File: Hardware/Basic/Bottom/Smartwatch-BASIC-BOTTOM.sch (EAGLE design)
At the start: 37 parts, among them U1 AD5242-SO16, U3 PCF8523

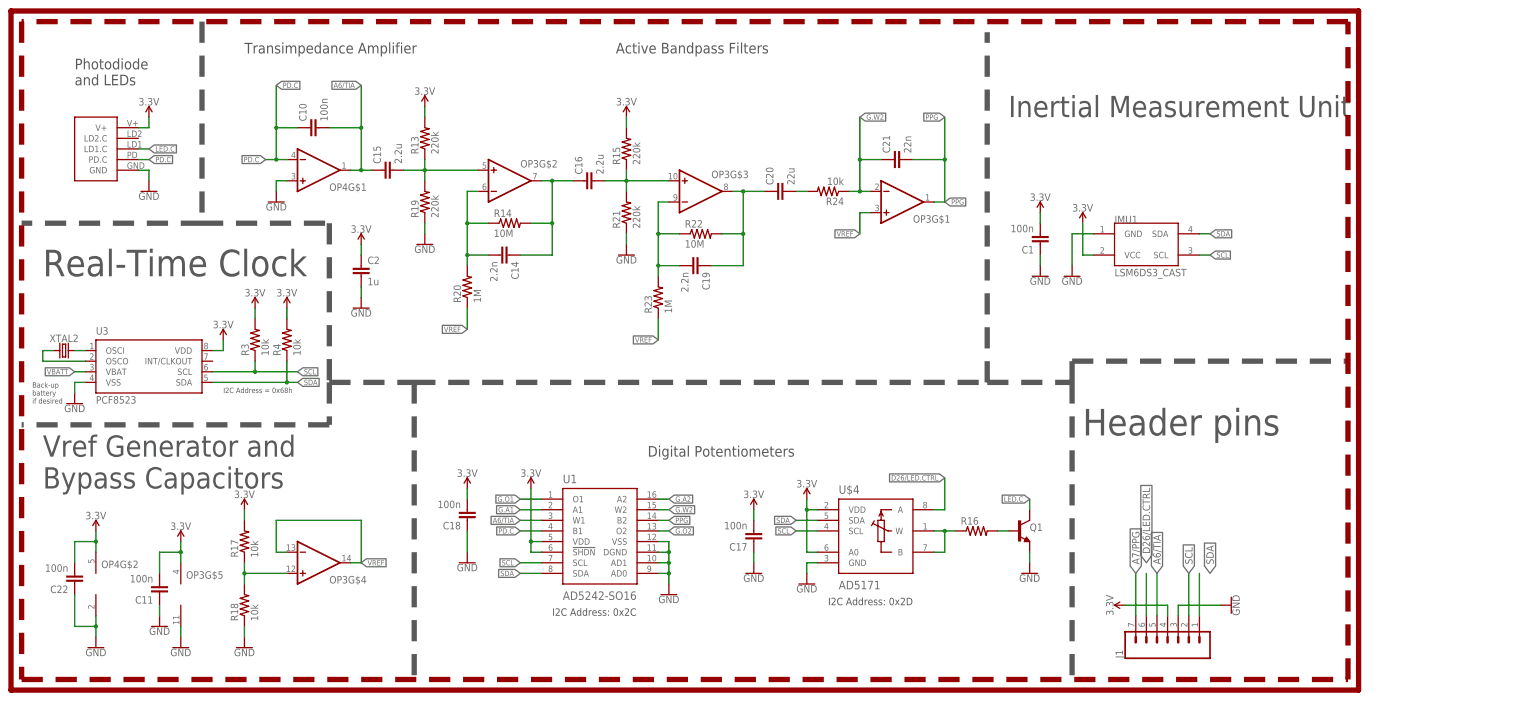
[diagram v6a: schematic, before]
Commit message: GPS Removed, added back original display, kept pads for adafruit display
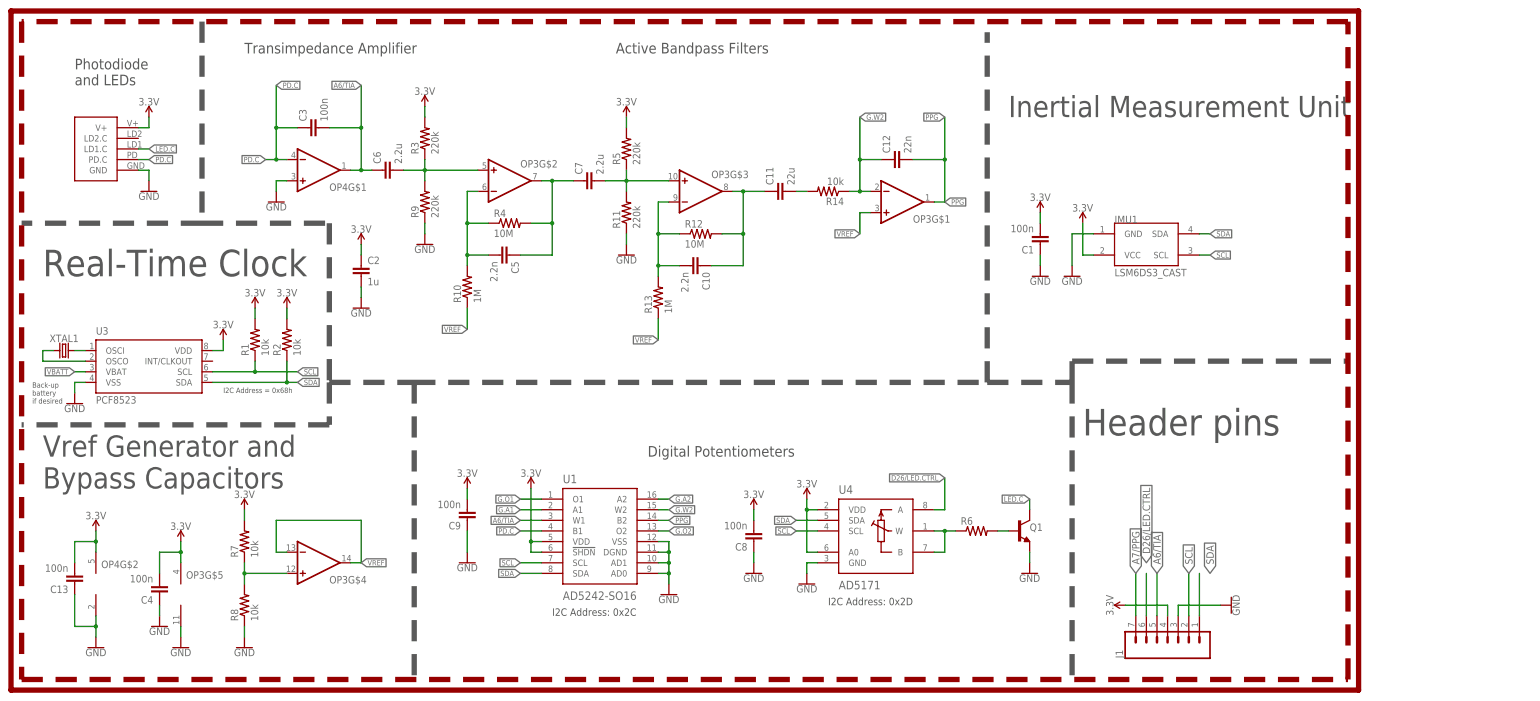
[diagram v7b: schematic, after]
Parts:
- removed C19: 2.2n, LinnesLab-Passives:CAPACITOR0603
- removed C20: 22u, LinnesLab-Passives:CAPACITOR0603
- removed R23: 1M, LinnesLab-Passives:RESISTOR0603
- removed R24: 10k, LinnesLab-Passives:RESISTOR0603
- added C3, C4: 100n, LinnesLab-Passives:CAPACITOR0603
- added R1, R2: 10k, LinnesLab-Passives:RESISTOR0603
- C10: value 100n -> 2.2n
- C11: value 100n -> 22u
- R13: value 220k -> 1M
- R14: value 10M -> 10k
- R3: value 10k -> 220k
- R4: value 10k -> 10M
- renumbered C14 to C5, C15 to C6, C16 to C7, C17 to C8, C18 to C9, C21 to C12, C22 to C13, R15 to R5, R16 to R6, R17 to R7, R18 to R8, R19 to R9, R20 to R10, R21 to R11, R22 to R12, U$3 to U2, U$4 to U4, XTAL2 to XTAL1
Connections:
- net 3.3V: now also C4.2, R1.2, R2.2; no longer C11.2, R13.2, R4.2
- net A6/TIA: now also C3.2; no longer C10.2
- net G.W2: now also R14.1; no longer R24.1
- net GND: now also C4.1; no longer C11.1
- net N$13: now also R3.1; no longer R13.1
- net N$15: now also R4.1; no longer R14.1
- net N$16: now also R4.2; no longer R14.2
- net N$18: now also C10.2, R13.2; no longer C19.2, R23.2
- net N$19: now also C10.1, C11.1; no longer C19.1, C20.1
- net N$20: now also C11.2, R14.2; no longer C20.2, R24.2
- net PD.C: now also C3.1; no longer C10.1
- net SCL: now also R1.1; no longer R3.1
- net SDA: now also R2.1; no longer R4.1
- net VREF: now also R13.1; no longer R23.1
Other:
- moved on the sheet: C10, C11, R13, R14, R3, R4
